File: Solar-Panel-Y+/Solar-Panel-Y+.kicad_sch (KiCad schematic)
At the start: 55 parts, among them J1 FFC2B28-10-G, U1 TSL2561, U2 Value

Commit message: Exported Gerbers
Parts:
- added H1, H2, H3, H4: MountingHole, MountingHole:MountingHole_2.2mm_M2_DIN965, symbol Mechanical:MountingHole
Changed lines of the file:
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@@
     (pin "2")
+  )
+  (symbol (lib_id "Mechanical:MountingHole") (at 192.405 130.302 0) (unit 1)
+    (in_bom yes) (on_board yes) (fields_autoplaced)
+    (property "Reference" "H4" (id 0) (at 194.945 129.4673 0)
+      (effects (font (size 1.27 1.27)) (justify left))
+    )
+    (property "Value" "MountingHole" (id 1) (at 194.945 132.0042 0)
+      (effects (font (size 1.27 1.27)) (justify left))
+    )
+    (property "Footprint" "MountingHole:MountingHole_2.2mm_M2_DIN965" (id 2) (at 192.405 130.302 0)
+      (effects (font (size 1.27 1.27)) hide)
+    )
+    (property "Datasheet" "~" (id 3) (at 192.405 130.302 0)
+      (effects (font (size 1.27 1.27)) hide)
+    )
   )
   (symbol (lib_id "Connector_Generic:Conn_02x05_Odd_Even") (at 290.322 149.098 0) (unit 1)
@@
     (pin "2")
   )
+  (symbol (lib_id "Mechanical:MountingHole") (at 192.278 111.506 0) (unit 1)
+    (in_bom yes) (on_board yes) (fields_autoplaced)
+    (property "Reference" "H1" (id 0) (at 194.818 110.6713 0)
+      (effects (font (size 1.27 1.27)) (justify left))
+    )
+    (property "Value" "MountingHole" (id 1) (at 194.818 113.2082 0)
+      (effects (font (size 1.27 1.27)) (justify left))
+    )
+    (property "Footprint" "MountingHole:MountingHole_2.2mm_M2_DIN965" (id 2) (at 192.278 111.506 0)
+      (effects (font (size 1.27 1.27)) hide)
+    )
+    (property "Datasheet" "~" (id 3) (at 192.278 111.506 0)
+      (effects (font (size 1.27 1.27)) hide)
+    )
+  )
+  (symbol (lib_id "Mechanical:MountingHole") (at 192.278 117.729 0) (unit 1)
+    (in_bom yes) (on_board yes) (fields_autoplaced)
+    (property "Reference" "H2" (id 0) (at 194.818 116.8943 0)
+      (effects (font (size 1.27 1.27)) (justify left))
+    )
+    (property "Value" "MountingHole" (id 1) (at 194.818 119.4312 0)
+      (effects (font (size 1.27 1.27)) (justify left))
+    )
+    (property "Footprint" "MountingHole:MountingHole_2.2mm_M2_DIN965" (id 2) (at 192.278 117.729 0)
+      (effects (font (size 1.27 1.27)) hide)
+    )
+    (property "Datasheet" "~" (id 3) (at 192.278 117.729 0)
+      (effects (font (size 1.27 1.27)) hide)
+    )
+  )
+  (symbol (lib_id "Mechanical:MountingHole") (at 192.278 123.952 0) (unit 1)
+    (in_bom yes) (on_board yes) (fields_autoplaced)
+    (property "Reference" "H3" (id 0) (at 194.818 123.1173 0)
+      (effects (font (size 1.27 1.27)) (justify left))
+    )
+    (property "Value" "MountingHole" (id 1) (at 194.818 125.6542 0)
+      (effects (font (size 1.27 1.27)) (justify left))
+    )
+    (property "Footprint" "MountingHole:MountingHole_2.2mm_M2_DIN965" (id 2) (at 192.278 123.952 0)
+      (effects (font (size 1.27 1.27)) hide)
+    )
+    (property "Datasheet" "~" (id 3) (at 192.278 123.952 0)
+      (effects (font (size 1.27 1.27)) hide)
+    )
+  )
   (sheet_instances
     (path "/" (page "1"))
@@
       (reference "D5") (unit 1) (value "SDM20U40-7") (footprint "Diode_SMD:D_SOD-523")
     )
+    (path "/9e70a67e-a0cb-4ed7-a04f-451f35eb0aa2"
+      (reference "H1") (unit 1) (value "MountingHole") (footprint "MountingHole:MountingHole_2.2mm_M2_DIN965")
+    )
+    (path "/a5e8c014-a02c-48a7-a56b-b148c03b0656"
+      (reference "H2") (unit 1) (value "MountingHole") (footprint "MountingHole:MountingHole_2.2mm_M2_DIN965")
+    )
+    (path "/f081c5ee-2d7c-454a-ae5e-f89b6ddc1d26"
+      (reference "H3") (unit 1) (value "MountingHole") (footprint "MountingHole:MountingHole_2.2mm_M2_DIN965")
+    )
+    (path "/0a3cbae7-b160-4bf5-bc29-b843867e2bbd"
+      (reference "H4") (unit 1) (value "MountingHole") (footprint "MountingHole:MountingHole_2.2mm_M2_DIN965")
+    )
     (path "/4860eced-eba7-4513-918e-cf78f7e1aa67"

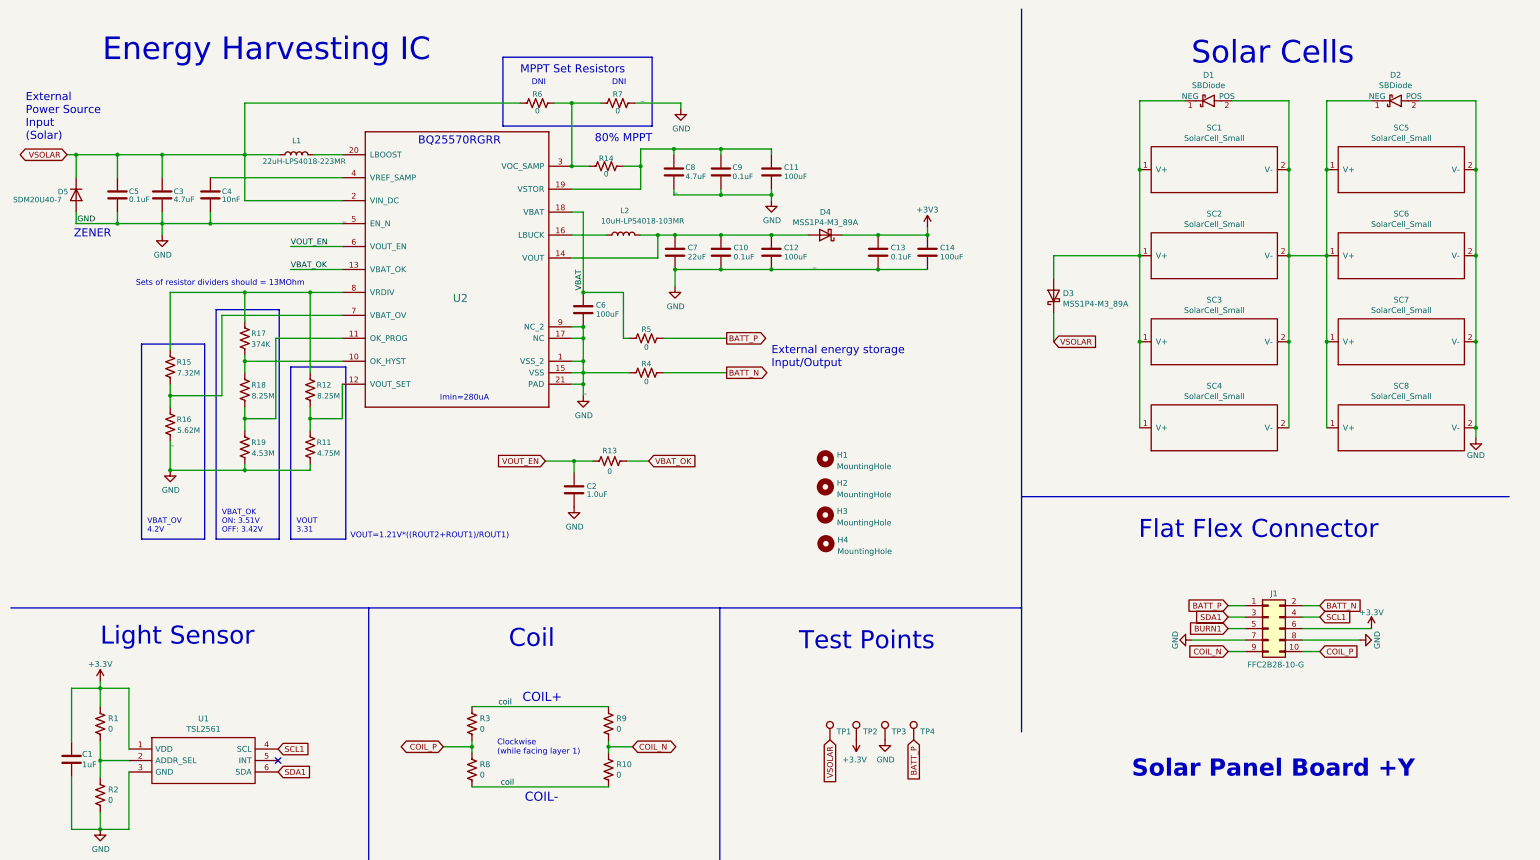
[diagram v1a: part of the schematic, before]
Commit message: Stack architecture schematic updates / fixes
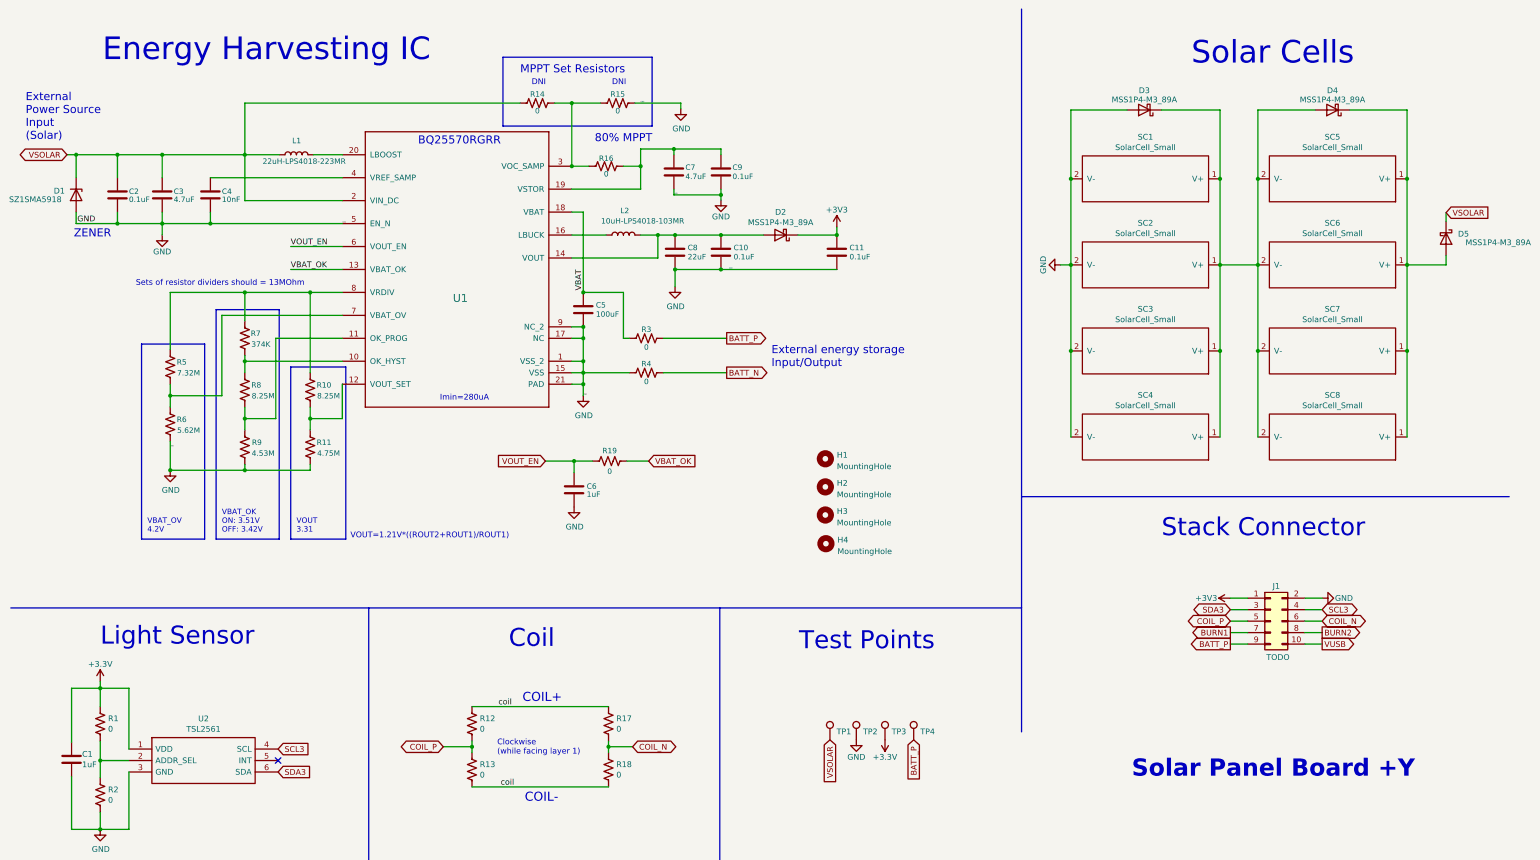
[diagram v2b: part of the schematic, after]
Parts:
- removed C11, C12: 100uF, Capacitor_SMD:C_0603_1608Metric, symbol Device:C
- removed C13: 0.1uF, Capacitor_SMD:C_0402_1005Metric, symbol Device:C
- removed D1, D2: SBDiode, solarpanels:SB Diode, symbol solarpanels:SBDiode
- removed D5: SDM20U40-7, Diode_SMD:D_SOD-523, symbol Device:D
- added D1: SZ1SMA5918, Diode_SMD:D_SMA, symbol Diode:Z1SMAxxx
- added D3, D4: MSS1P4-M3_89A, solarpanels:MICROSMP, symbol Device:D_Schottky
- C1, C10, C3, C4, C9: footprint Capacitor_SMD:C_0402_1005Metric -> Capacitor_SMD:C_0603_1608Metric
- C11: renamed from C14; value 100uF -> 0.1uF
- C2: renamed from C5; footprint Capacitor_SMD:C_0402_1005Metric -> Capacitor_SMD:C_0603_1608Metric
- C5: renamed from C6; footprint Capacitor_SMD:C_0603_1608Metric -> Capacitor_SMD:C_0805_2012Metric
- C6: renamed from C2; value 1.0uF -> 1uF; footprint Capacitor_SMD:C_0402_1005Metric -> Capacitor_SMD:C_0603_1608Metric
- C7: renamed from C8; footprint Capacitor_SMD:C_0402_1005Metric -> Capacitor_SMD:C_0603_1608Metric
- C8: renamed from C7; footprint Capacitor_SMD:C_0402_1005Metric -> Capacitor_SMD:C_0603_1608Metric
- J1: value FFC2B28-10-G -> TODO
- R1, R11, R2, R4: footprint Resistor_SMD:R_0402_1005Metric -> Resistor_SMD:R_0603_1608Metric
- R10: renamed from R12; footprint Resistor_SMD:R_0402_1005Metric -> Resistor_SMD:R_0603_1608Metric
- R12: renamed from R3; footprint Resistor_SMD:R_0402_1005Metric -> Resistor_SMD:R_0603_1608Metric
- R13: renamed from R8; footprint Resistor_SMD:R_0402_1005Metric -> Resistor_SMD:R_0603_1608Metric
- R14: renamed from R6; footprint Resistor_SMD:R_0402_1005Metric -> Resistor_SMD:R_0603_1608Metric
- R15: renamed from R7; footprint Resistor_SMD:R_0402_1005Metric -> Resistor_SMD:R_0603_1608Metric
- R16: renamed from R14; footprint Resistor_SMD:R_0402_1005Metric -> Resistor_SMD:R_0603_1608Metric
- R17: renamed from R9; footprint Resistor_SMD:R_0402_1005Metric -> Resistor_SMD:R_0603_1608Metric
- R18: renamed from R10; footprint Resistor_SMD:R_0402_1005Metric -> Resistor_SMD:R_0603_1608Metric
- R19: renamed from R13; footprint Resistor_SMD:R_0402_1005Metric -> Resistor_SMD:R_0603_1608Metric
- R3: renamed from R5; footprint Resistor_SMD:R_0402_1005Metric -> Resistor_SMD:R_0603_1608Metric
- R5: renamed from R15; footprint Resistor_SMD:R_0402_1005Metric -> Resistor_SMD:R_0603_1608Metric
- R6: renamed from R16; footprint Resistor_SMD:R_0402_1005Metric -> Resistor_SMD:R_0603_1608Metric
- R7: renamed from R17; footprint Resistor_SMD:R_0402_1005Metric -> Resistor_SMD:R_0603_1608Metric
- R8: renamed from R18; footprint Resistor_SMD:R_0402_1005Metric -> Resistor_SMD:R_0603_1608Metric
- R9: renamed from R19; footprint Resistor_SMD:R_0402_1005Metric -> Resistor_SMD:R_0603_1608Metric
- renumbered D4 to D2, D3 to D5, SC5 to SC1, SC6 to SC2, SC7 to SC3, SC8 to SC4, SC1 to SC5, SC2 to SC6, SC3 to SC7, SC4 to SC8, U2 to U1, U1 to U2
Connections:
- net +3V3: now also J1.1 (Pin_1), TP3.1; no longer J1.6 (Pin_6), TP2.1
- net BATT_N: no longer J1.2 (Pin_2)
- net BATT_P: now also J1.9 (Pin_9); no longer J1.1 (Pin_1)
- net BURN1: now also J1.7 (Pin_7); no longer J1.5 (Pin_5)
- net COIL_N: now also J1.6 (Pin_6); no longer J1.9 (Pin_9)
- net COIL_P: now also J1.5 (Pin_5); no longer J1.10 (Pin_10)
- net GND: now also J1.2 (Pin_2), TP2.1, D1.2 (A), D3.2 (A); no longer J1.7 (Pin_7), J1.8 (Pin_8), TP3.1
- net VSOLAR: now also D1.1 (K)
- net at D5.2 (A), SC5.1 (V+), SC6.1 (V+)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: now also D4.1 (K)
- net at SC1.1 (V+), SC2.1 (V+), SC3.1 (V+)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: now also D3.1 (K), D4.2 (A)
- net SCL1 renamed SCL3
- net SDA1 renamed SDA3
- new net BURN2: J1.8 (Pin_8)
- new net VUSB: J1.10 (Pin_10)
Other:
- note added: "Stack Connector"
- note removed: "Flat Flex Connector"
- moved on the sheet: C11, D2, D5, SC1, SC2, SC3, SC4, SC5, SC6, SC7, SC8

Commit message: X / Y+ board updates v04
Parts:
- removed R4: 0, Resistor_SMD:R_0603_1608Metric, symbol Device:R_US
- added C12, C13: 10nF, Capacitor_SMD:C_0402_1005Metric, symbol Device:C
- added Q1, Q3: BSS138DWQ-7, Package_TO_SOT_SMD:SOT-363_SC-70-6, symbol mainboard:BSS138DWQ-7
- added Q2, Q4: MBT2222ADW1T1, Package_TO_SOT_SMD:SOT-363_SC-70-6, symbol Transistor_BJT:MBT2222ADW1T1
- added R20, R27: 680, Resistor_SMD:R_0402_1005Metric, symbol Device:R_US
- added R21, R28: 100K, Resistor_SMD:R_0402_1005Metric, symbol Device:R_US
- added R22, R23: 0, Resistor_SMD:R_0402_1005Metric, symbol Device:R_US
- added R24, R25, R29, R30: 10K, Resistor_SMD:R_0402_1005Metric, symbol Device:R_US
- added R26, R31: 200K, Resistor_SMD:R_0402_1005Metric, symbol Device:R_US
- C1, C10, C11, C2, C3, C4, C6, C7, C8, C9: footprint Capacitor_SMD:C_0603_1608Metric -> Capacitor_SMD:C_0402_1005Metric
- D1: value SZ1SMA5918 -> SZMM5Z5V1T1G; footprint Diode_SMD:D_SMA -> Diode_SMD:D_SOD-523
- H1, H2, H3, H4: footprint MountingHole:MountingHole_2.2mm_M2_DIN965 -> MountingHole:MountingHole_2.2mm_M2_DIN965_Pad; symbol Mechanical:MountingHole -> Mechanical:MountingHole_Pad
- J1: footprint solarpanels:GCT_FFC2B28-10-G -> Connector_PinHeader_1.27mm:PinHeader_2x05_P1.27mm_Vertical_SMD
- R1, R10, R11, R12, R13, R14, R15, R16, R17, R18, R19, R2, R3, R5, R6, R7, R8, R9: footprint Resistor_SMD:R_0603_1608Metric -> Resistor_SMD:R_0402_1005Metric
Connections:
- net +3V3: now also R21.1, R24.1, R25.1, R28.1, R29.1, R30.1
- net BATT_P: no longer TP4.1
- net GND: now also H1.1, H2.1, H3.1, H4.1, C12.2, C13.2, Q1.1 (S2), Q1.4 (S1), Q3.1 (S2), Q3.4 (S1)
- net SCL3: now also Q2.1 (E1), Q2.3 (C2), R22.2; no longer U2.4 (SCL)
- net SDA3: now also Q4.1 (E1), Q4.3 (C2), R23.2; no longer U2.6 (SDA)
- net VBAT: now also TP4.1
- new net: Q4.2 (B1), R27.1
- new net: Q3.6 (D1), Q4.5 (B2), R27.2, R29.2
- new net: Q1.6 (D1), Q2.5 (B2), R20.2, R24.2
- new net: Q1.2 (G2), Q1.3 (D2), R21.2
- new net: C12.1, Q1.5 (G1), R26.2
- new net: C13.1, Q3.5 (G1), R31.2
- new net: Q3.2 (G2), Q3.3 (D2), R28.2
- new net: Q2.2 (B1), R20.1
- new net SCL_LS: Q2.4 (E2), Q2.6 (C1), R22.1, R25.2, R26.1, U2.4 (SCL)
- new net SDA_LS: Q4.4 (E2), Q4.6 (C1), R23.1, R30.2, R31.1, U2.6 (SDA)
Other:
- note added: "I2C Bus Protection - Light Sensor"
- moved on the sheet: C10, C11, C2, C3, C4, C5, C6, C7, C8, C9, D1, D2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

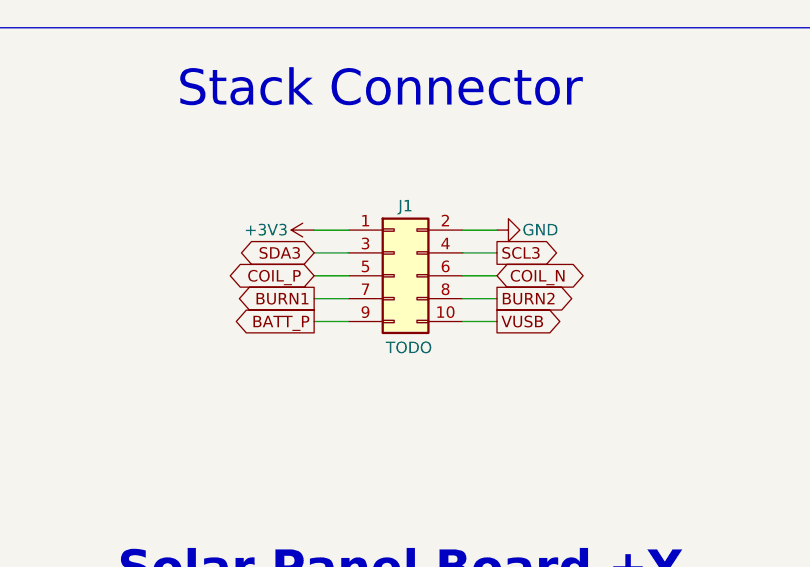
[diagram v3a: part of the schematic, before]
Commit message: Re-check boards, fixed connector pinouts, moved Y+ connector, re-export models
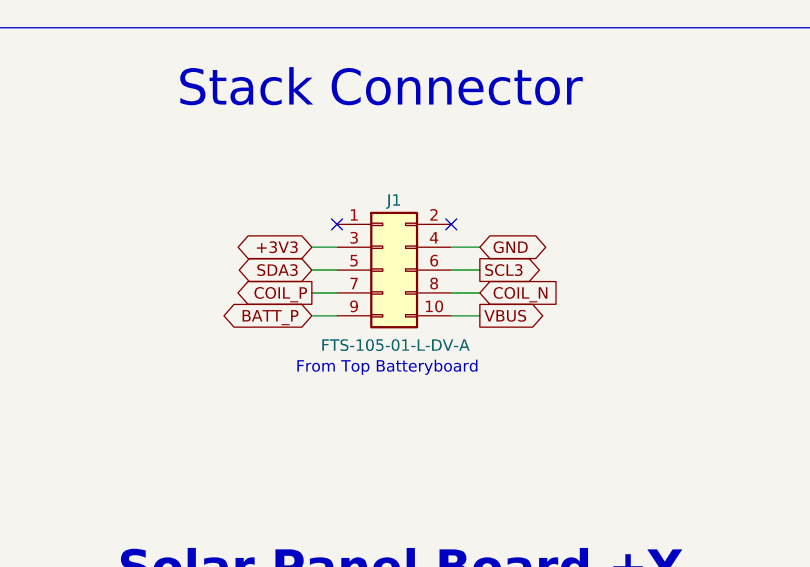
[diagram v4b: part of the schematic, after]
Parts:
- J1: value TODO -> FTS-105-01-L-DV-A; footprint Connector_PinHeader_1.27mm:PinHeader_2x05_P1.27mm_Vertical_SMD -> batteryboard:FTS-105-XX-YY-DV-A
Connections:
- net BURN1 is gone; now on net COIL_P: J1.7 (Pin_7)
- net BURN2 is gone; now on net COIL_N: J1.8 (Pin_8)
- net +3V3: now also J1.3 (Pin_3); no longer J1.1 (Pin_1)
- net COIL_N: no longer J1.6 (Pin_6)
- net COIL_P: no longer J1.5 (Pin_5)
- net GND: now also J1.4 (Pin_4); no longer J1.2 (Pin_2)
- net SCL3: now also J1.6 (Pin_6); no longer J1.4 (Pin_4)
- net SDA3: now also J1.5 (Pin_5); no longer J1.3 (Pin_3)
- net VUSB renamed VBUS
- no-connect marks 1 -> 3
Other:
- note added: "From Top Batteryboard"
- moved on the sheet: J1

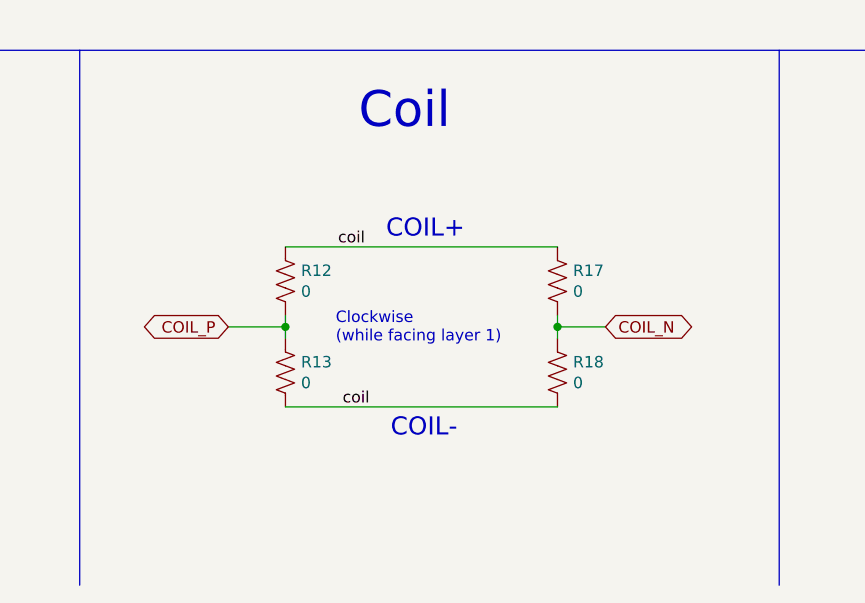
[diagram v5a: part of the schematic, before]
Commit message: Modified coil resistors to allow only one to be populated
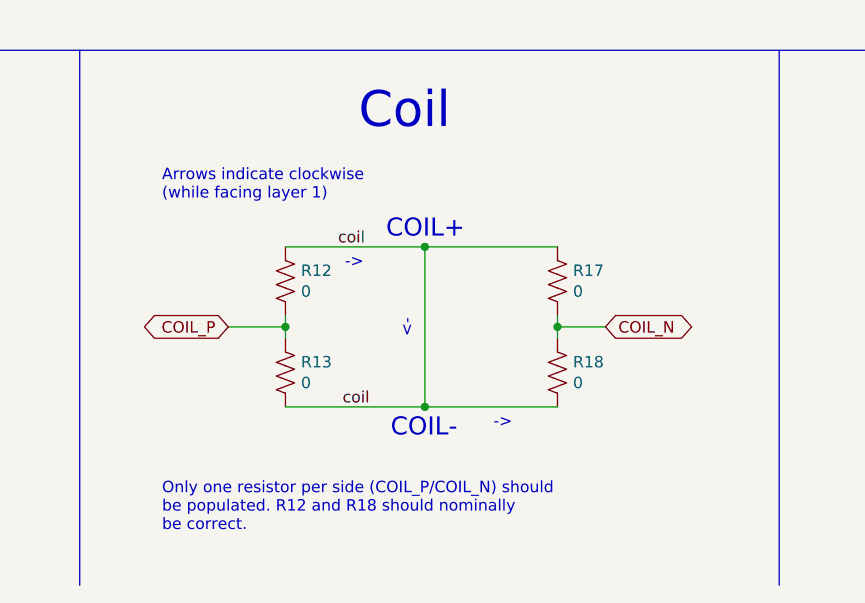
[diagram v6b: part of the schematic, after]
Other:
- note added: "->"
- note added: "<-"
- note added: "Arrows indicate clockwise (while facing layer 1)"
- note added: "Only one resistor per side (COIL_P/COIL_N) should be populated. R12 and R18 should nominally be correct."
- note removed: "Clockwise (while facing layer 1)"
